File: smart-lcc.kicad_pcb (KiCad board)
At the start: 4 copper layers, 53.2 x 53.2 mm, 117 parts, among them J1 280372-1, J2 F0503-ZV-24-20T-R, J3 Conn_01x24, J4 BM04B-SRSS-TB(LF)(SN), J5 BM04B-SRSS-TB(LF)(SN), J6 Micro_SD_Card_Det2, J7 Conn_01x12, J8 BM04B-SRSS-TB(LF)(SN), Q1 2N7002, Q2 2N7002, Q4 2N7002, Q6 NTGD3148NT1G, SW1 SW_Push, SW2 SW_Push, U1 LM5050-1, U2 RP2040, U3 ESP32-S3-WROOM-1, U4 W25Q16JVSNIQ (Program Flash), U5 W25Q16JVSNIQ (Opt. Settings f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, U6 TPS82130, U7 74LVC1G125, U8 LM5050-1, Y1 XYDBPCNANF-12MHZ

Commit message: Added some very basic ordering information (more soon)
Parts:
- R26, R27: value 18K -> 18K7
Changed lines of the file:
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@@
     (descr "Resistor SMD 0402 (1005 Metric), square (rectangular) end terminal, IPC_7351 nominal, (Body size source: IPC-SM-782 page 72, https://www.pcb-3d.com/wordpress/wp-content/uploads/ipc-sm-782a_amendment_1_and_2.pdf), generated with kicad-footprint-generator")
     (tags "resistor")
+    (property "LCSC" "C102855")
     (property "Sheetfile" "smart-lcc.kicad_sch")
     (property "Sheetname" "")
@@
         (effects (font (size 1 1) (thickness 0.15)))
     )
-    (fp_text value "18K" (at 0 1.17) (layer "F.Fab")
+    (fp_text value "18K7" (at 0 1.17) (layer "F.Fab")
         (effects (font (size 1 1) (thickness 0.15)))
     )
@@
     (descr "Resistor SMD 0402 (1005 Metric), square (rectangular) end terminal, IPC_7351 nominal, (Body size source: IPC-SM-782 page 72, https://www.pcb-3d.com/wordpress/wp-content/uploads/ipc-sm-782a_amendment_1_and_2.pdf), generated with kicad-footprint-generator")
     (tags "resistor")
+    (property "LCSC" "C102855")
     (property "Sheetfile" "smart-lcc.kicad_sch")
     (property "Sheetname" "")
@@
         (effects (font (size 1 1) (thickness 0.15)))
     )
-    (fp_text value "18K" (at 0 1.17 90) (layer "F.Fab")
-        (effects (font (size 1 1) (thickness 0.15)))
-    )
+    (fp_text value "18K7" (at 0 1.17 90) (layer "F.Fab")
+        (effects (font (size 1 1) (thickness 0.15)))
+    )

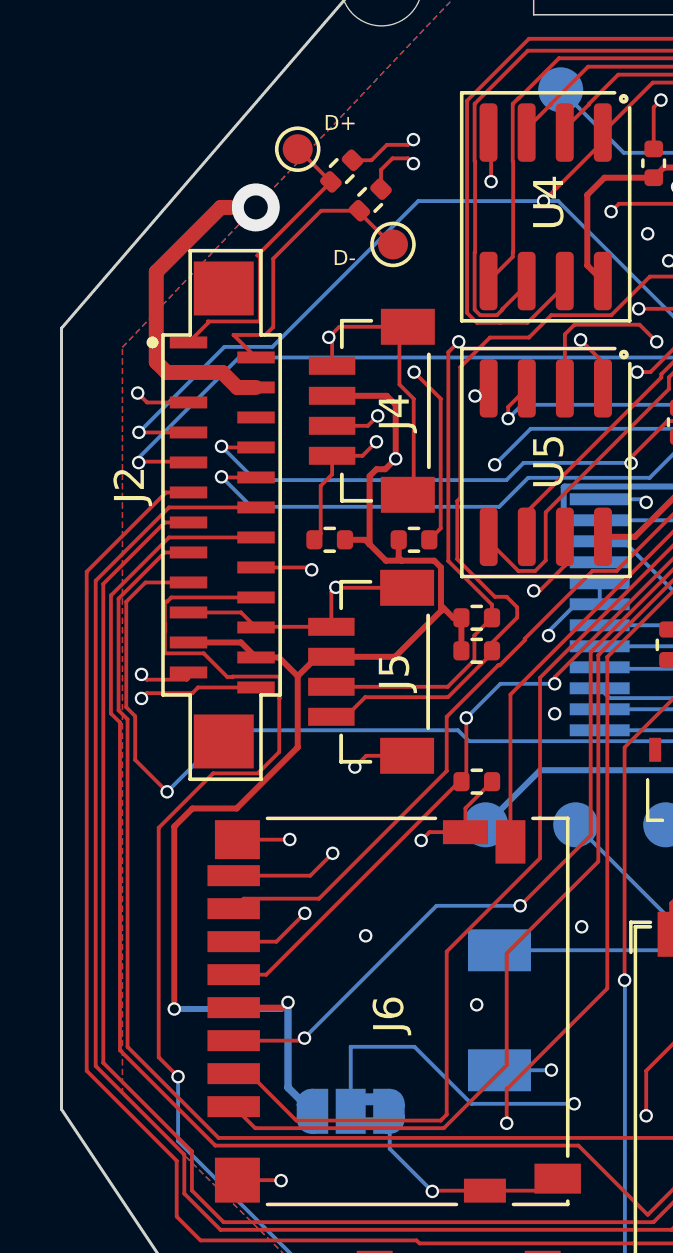
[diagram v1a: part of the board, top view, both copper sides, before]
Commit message: Updated to use a more flexible FPC connector footprint
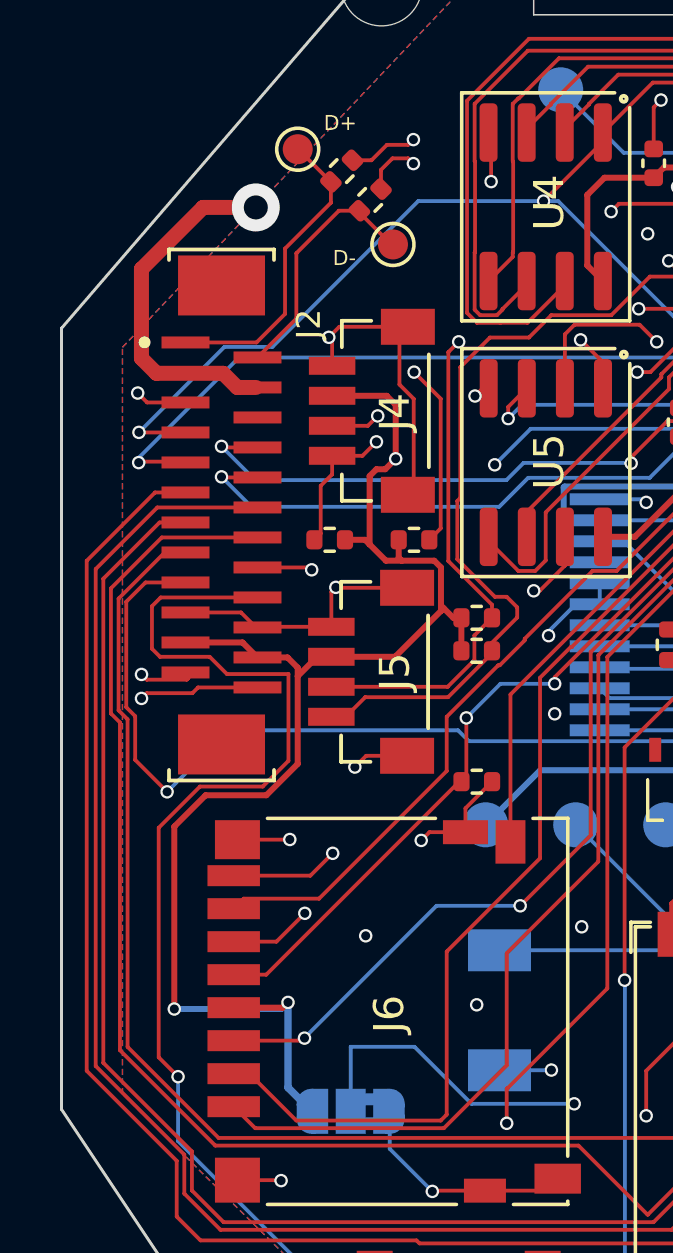
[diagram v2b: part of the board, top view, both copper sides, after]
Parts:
- J2: footprint 2N7002:FPC_24 -> FlexibleFPC:Flexible24Pin
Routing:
- net RP2040_USB_DN: track 9.94 -> 8.33 mm
- net ESP32_EN: track 88.2 -> 89.7 mm
- net VIN_DEBUG: track 66.1 -> 67.1 mm
- net +3V3: track 291.4 -> 292.0 mm

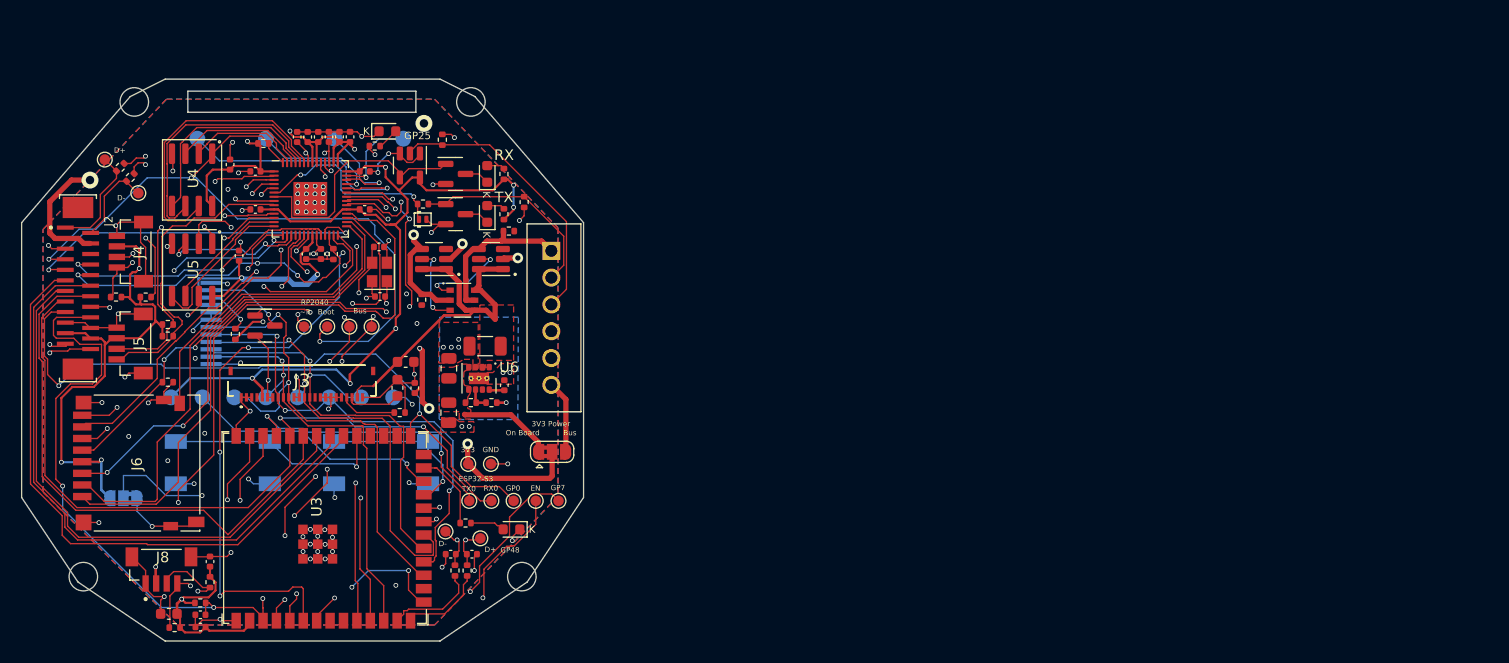
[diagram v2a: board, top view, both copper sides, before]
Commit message: R3A (preliminary)
Changes:
* Switched the OLED connector for an EyeSPI connector (feature parity with APEC)
* Removed the need for a debug board by moving USB connectors and SWD/JTAG ports to this board
* Move to 6 layers
* Component changes for a more dense design
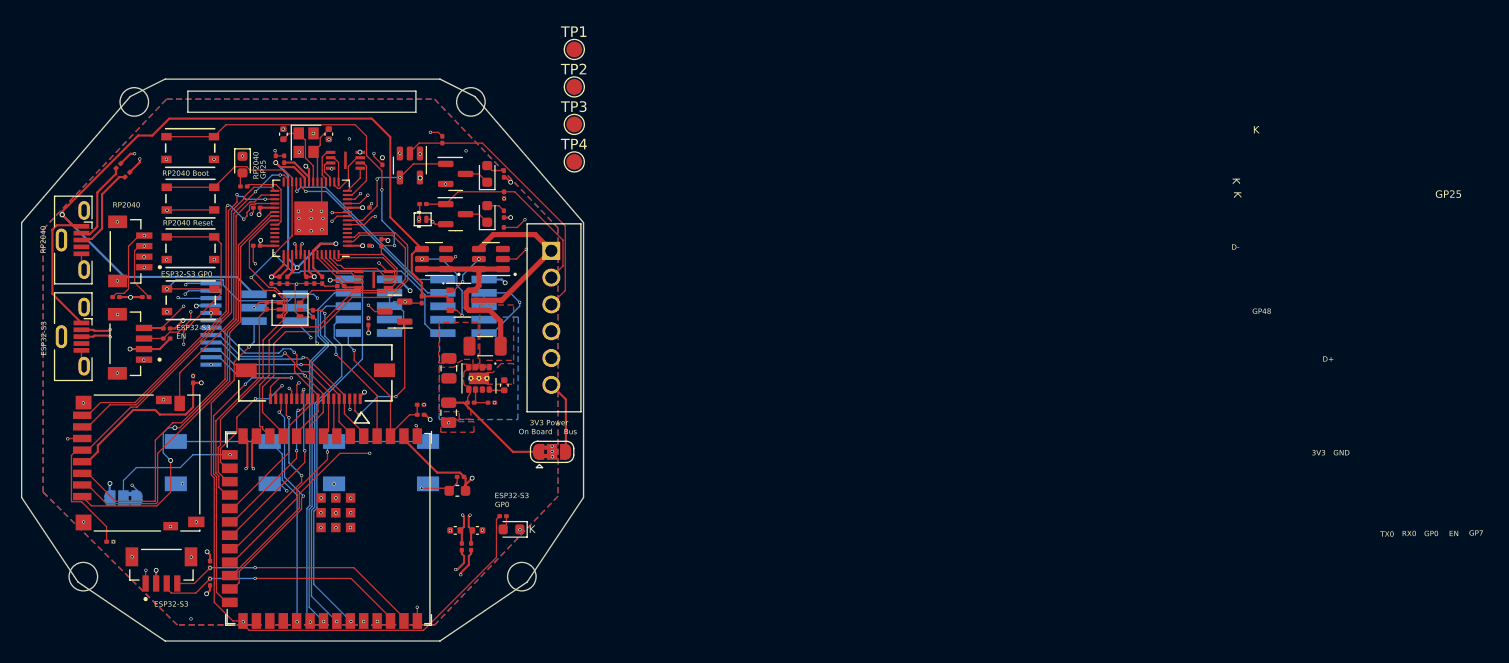
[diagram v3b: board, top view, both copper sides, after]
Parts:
- removed C1, C3: 2.2 µF / 25V, Capacitor_SMD:C_0603_1608Metric
- removed C4: 1 uF, 16V, Capacitor_SMD:C_0402_1005Metric
- removed TP10, TP28, TP29, TP5, TP6, TP7, TP8, TP9: TestPoint_Small, TestPoint:TestPoint_Pad_D1.0mm
- removed TP13, TP17, TP18: TestPoint, TestPoint:TestPoint_Pad_D1.0mm
- removed TP14, TP15, TP16, TP19: TestPoint, TestPoint:TestPoint_Pad_D1.5mm
- removed TP20, TP21, TP22, TP23, TP24, TP25, TP26, TP27: TestPoint_Small, TestPoint:TestPoint_Pad_D1.5mm
- added J10: Conn_02x05_Odd_Even, Connector_PinHeader_1.27mm:PinHeader_2x05_P1.27mm_Vertical_SMD, B.Cu at (55.8, 44.4)
- added J11: Conn_02x03_Odd_Even, Connector_PinHeader_1.27mm:PinHeader_2x03_P1.27mm_Vertical_SMD, B.Cu at (46.8, 44.5)
- added J12: Conn_01x12, TFT_1.47IN_172X320_12P:TFT_1.47IN_172X320_12P, B.Cu at (49.8, 46.0)
- added J9: Molex_0525591853, Molex_5051101892:CON_5051101892_MOL, F.Cu at (50.7, 50.7)
- added Q3: 2N7002, Package_TO_SOT_SMD:SOT-23, F.Cu at (58.2, 44.9)
- added REF**: VariegatedCoffeeLogo_Small, VariegatedCoffeeLogo:VariegatedCoffeeLogo_Small, B.Cu at (43.3, 75.8)
- added REF**: OSHW-Logo2_9.8x8mm_SilkScreen, Symbol:OSHW-Logo2_9.8x8mm_SilkScreen, B.Cu at (56.2, 70.2)
- added SW3: SW_Push, ul_PTS815-SJM-250-SMTR-LFS:SW4_PTS815 SJM 250 SMTR LFS_CNK, F.Cu at (38.8, 29.4)
- added SW4: SW_Push, ul_PTS815-SJM-250-SMTR-LFS:SW4_PTS815 SJM 250 SMTR LFS_CNK, F.Cu at (38.9, 34.2)
- added SW5: SW_Push, ul_PTS815-SJM-250-SMTR-LFS:SW4_PTS815 SJM 250 SMTR LFS_CNK, F.Cu at (38.9, 38.9)
- added SW6: SW_Push, ul_PTS815-SJM-250-SMTR-LFS:SW4_PTS815 SJM 250 SMTR LFS_CNK, F.Cu at (38.9, 43.8)
- C10, C13, C14, C15, C16, C17, C18, C19, C20, C21, C22, C24, C9: footprint Capacitor_SMD:C_0402_1005Metric -> Capacitor_SMD:C_0201_0603Metric
- C11, C12, C23, C8: value 1 uF, 16V -> 1 uF, 10V; footprint Capacitor_SMD:C_0402_1005Metric -> Capacitor_SMD:C_0201_0603Metric
- J2: value F0503-ZV-24-20T-R -> USB_B_Micro; footprint FlexibleFPC:Flexible24Pin -> Connector_USB:USB_Micro-B_Molex-105133-0001
- J3: value Conn_01x24 -> USB_B_Micro; footprint FH34SRJ-24S-0.5SH_50:FH34SRJ24S05SH50 -> Connector_USB:USB_Micro-B_Molex-105133-0001
- J7: value Conn_01x12 -> Conn_02x05_Odd_Even; footprint TFT_1.47IN_172X320_12P:TFT_1.47IN_172X320_12P -> Connector_PinHeader_1.27mm:PinHeader_2x05_P1.27mm_Vertical_SMD
- Q4: value 2N7002 -> DMN63D8LDW; footprint Package_TO_SOT_SMD:SOT-23 -> PCM_Package_TO_SOT_SMD_AKL:SOT-363_SC-70-6
- R1: value 910K -> 100R; footprint Resistor_SMD:R_0402_1005Metric -> Resistor_SMD:R_0201_0603Metric
- R10, R11, R13, R14, R15, R16, R17, R19, R2, R20, R21, R22, R23, R24, R25, R26, R27, R3, R4, R5, R6, R7, R8, R9: footprint Resistor_SMD:R_0402_1005Metric -> Resistor_SMD:R_0201_0603Metric
- R12: value 100R -> 10R; footprint Resistor_SMD:R_0402_1005Metric -> Resistor_SMD:R_0201_0603Metric
- R18: value 10R -> 4K7; footprint Resistor_SMD:R_0402_1005Metric -> Resistor_SMD:R_0201_0603Metric
- TP1, TP2, TP3, TP4: value TestPoint_Small -> TestPoint; footprint TestPoint:TestPoint_Pad_D1.0mm -> TestPoint:TestPoint_Pad_D1.5mm
- U4, U5: footprint PCM_Package_SO_AKL:SOIC-8_3.9x4.9mm_P1.27mm -> W25Q16JVUXIQ:SON50P300X200X60-9N
- moved TP1 43.5 mm to (75.2, 20.1)
- moved TP2 40.4 mm to (75.2, 23.6)
- moved TP3 36.1 mm to (75.2, 27.1)
- moved TP4 32.3 mm to (75.2, 30.7)
- moved C28 29.7 mm to (64.1, 61.9)
- moved C12 28.8 mm to (60.6, 53.7), turned to 180 degrees
- moved C24 28.4 mm to (64.4, 60.5)
- moved R9 27.4 mm to (60.6, 54.6), turned to 180 degrees
- moved J3 22.1 mm to (27.7, 47.2), turned to -90 degrees
- moved R12 21.2 mm to (55.7, 45.8), turned to 90 degrees
- moved U4 19.6 mm to (56.2, 41.8), turned to 180 degrees
- moved C7 17.9 mm to (47.6, 28.1), turned to 90 degrees
- moved U5 17.8 mm to (53.5, 30.6), turned to 0 degrees
- moved C8 17.3 mm to (39.1, 51.3)
- moved C10 16.2 mm to (57.0, 30.7), turned to 90 degrees
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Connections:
- net 12V_OLED renamed VIN_CONN
- J2 pad 1: RP2040_USB_DP -> VIN_DEBUG
- J2 pad 3: VIN_DEBUG -> RP2040_USB_DP
- J2 pad 4: VIN_DEBUG -> unconnected-(J2-ID-Pad4)
- J2 pad 6: unconnected-(J2-Pin_6-Pad6) -> GND
- J3 pad 1: GND -> VIN_DEBUG
- J3 pad 2: GND -> ESP32_USB_DN
- J3 pad 3: GND -> ESP32_USB_DP
- J3 pad 5: +3V3 -> GND
- J7 pad 1: GND -> +3V3
- J7 pad 10: SSD1309_MOSI -> RP2040_RESETn
- J7 pad 2: Net-(J7-Pin_2) -> RP2040_SWD
- J7 pad 3: Net-(J7-Pin_3) -> GND
- J7 pad 4: +3V3 -> RP2040_SWCLK
- J7 pad 6: GND -> unconnected-(J7-Pin_6-Pad6)
- J7 pad 7: SSD1309_DC -> unconnected-(J7-Pin_7-Pad7)
- J7 pad 8: SSD1309_CS -> unconnected-(J7-Pin_8-Pad8)
- J7 pad 9: SSD1309_SCLK -> GND
- Q4 pad 1: BACKLIGHT -> GND
- Q4 pad 2: GND -> ESP32_BOOTSEL_RP2040
- Q4 pad 3: Net-(J7-Pin_2) -> RP2040_RESETn
- R1 pad 1: GND -> ESP32_GPIO0
- R1 pad 2: Net-(J3-Pin_21) -> Net-(D4-A)
- R11 pad 1: RP2040_RESETn -> ESP32_BOOTSEL_RP2040
- R12 pad 1: Net-(U3-GPIO48/SPICLK_N/SUBSPICLK_N_DIFF) -> +3V3
- R12 pad 2: Net-(D4-A) -> Net-(J12-Pin_3)
- R18 pad 1: +3V3 -> ESP32_DISABLE_RP2040
- R18 pad 2: Net-(J7-Pin_3) -> GND
- TP1 pad 1: ESP32_RXD0 -> unconnected-(TP1-Pad1)
- TP2 pad 1: ESP32_TXD0 -> unconnected-(TP2-Pad1)
- TP3 pad 1: ESP32_GPIO0 -> unconnected-(TP3-Pad1)
- TP4 pad 1: ESP32_EN -> unconnected-(TP4-Pad1)
- U2 pad 18: unconnected-(U2-GPIO15-Pad18) -> RP2040_SET_CS
- U2 pad 28: RP2040_SET_CS -> unconnected-(U2-GPIO17-Pad28)
- U2 pad 38: Net-(U2-GPIO26_ADC0) -> unconnected-(U2-GPIO26_ADC0-Pad38)
- U2 pad 39: Net-(U2-GPIO27_ADC1) -> unconnected-(U2-GPIO27_ADC1-Pad39)
- U2 pad 4: RP2040_ESP32_CTS -> unconnected-(U2-GPIO2-Pad4)
- U2 pad 40: Net-(U2-GPIO28_ADC2) -> unconnected-(U2-GPIO28_ADC2-Pad40)
- U2 pad 41: Net-(U2-GPIO29_ADC3) -> unconnected-(U2-GPIO29_ADC3-Pad41)
- U2 pad 5: RP2040_ESP32_RTS -> unconnected-(U2-GPIO3-Pad5)
- U3 pad 10: RP2040_ESP32_RX -> SSD1309_CS
- U3 pad 11: RP2040_ESP32_TX -> RP2040_ESP32_RX
- U3 pad 12: SSD1309_RES -> RP2040_ESP32_TX
- U3 pad 17: SSD1309_DC -> RP2040_SERIAL_BOOT
- U3 pad 18: SSD1309_CS -> ESP32_BOOTSEL_RP2040
- U3 pad 19: SSD1309_MOSI -> ESP32_EYESPI_SD_CS
- U3 pad 20: SSD1309_SCLK -> ESP32_EYESPI_MEM_CS
- U3 pad 21: RP2040_ESP32_RTS -> ESP32_EYESPI_TS_CS
- U3 pad 22: RP2040_ESP32_CTS -> ESP32_EYESPI_INT
- U3 pad 25: Net-(U3-GPIO48/SPICLK_N/SUBSPICLK_N_DIFF) -> ESP32_EYESPI_BUSY_TE
- U3 pad 4: RP2040_RESETn -> ESP32_DISABLE_RP2040
- U3 pad 5: RP2040_BOOTSEL -> SSD1309_SCLK
- U3 pad 6: RP2040_SERIAL_BOOT -> SSD1309_MOSI
- U3 pad 7: Net-(U3-GPIO7/TOUCH7/ADC1_CH6) -> ESP32_GPIO7
- U3 pad 8: ESP32_RTS0 -> SSD1309_DC
- U3 pad 9: ESP32_CTS0 -> SSD1309_RES
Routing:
- net +3V3: track 292.0 -> 75.8 mm, vias 20 -> 33
- net GND: track 173.6 -> 80.4 mm, vias 93 -> 87
- net ESP32_EN: track 89.7 -> 42.9 mm, vias 4 -> 3
- net RP2040_BOOTSEL: track 96.8 -> 50.8 mm, vias 6 -> 2
- net RP2040_ESP32_RTS: track 41.9 -> 0.00 mm, vias 2 -> 0
- net RP2040_ESP32_CTS: track 41.4 -> 0.00 mm, vias 2 -> 0
- net ESP32_RXD0: track 73.2 -> 32.9 mm
- net RP2040_SERIAL_BOOT: track 64.1 -> 31.2 mm, vias 5 -> 0
- net ESP32_GPIO45: track 0.00 -> 30.8 mm, vias 0 -> 2
- net Net-(U3-GPIO7/TOUCH7/ADC1_CH6): track 30.4 -> 0.00 mm, vias 2 -> 0
- net RP2040_SD_DAT1: track 63.8 -> 33.9 mm
- net SSD1309_DC: track 48.8 -> 19.0 mm, vias 2 -> 1
- net Net-(JP1-C): track 40.6 -> 12.8 mm, vias 3 -> 1
- net RP2040_ESP32_TX: track 61.9 -> 34.5 mm, vias 4 -> 0
- net SSD1309_CS: track 45.1 -> 18.0 mm, vias 3 -> 1
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- added copper zone on In1.Cu, net +3V3
- added copper zone on In3.Cu, net GND
- added copper zone on In4.Cu, net GND
- removed copper zone on In1.Cu, net GND
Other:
- copper layers 4 -> 6
- board text added: "ESP-Debug"
- board text added: "ESP32 JTAG"
- board text added: "ESP32-S3 EN"
- board text added: "ESP32-S3 GP0"
- board text added: "RP2040 Boot"
- board text added: "RP2040 Reset"
- board text added: "RP2040 SWD"
- board text added: "Rev R3A"
- board text added: "variegated.coffee/open-lcc"
- board text removed: "BL"
- board text removed: "Boot"
- board text removed: "CK"
- board text removed: "CS"
- board text removed: "DC"
- board text removed: "GP26"
- board text removed: "GP27"
- board text removed: "GP28"
- board text removed: "GP29"
- board text removed: "Licensed under CERN-OHL-P v2"
- board text removed: "MO"
- board text removed: "RES"
- board text removed: "RP2040 GPIO"
- board text removed: "Rev R2C"
- board text removed: "github.com/open-lcc/open-lcc-board"
- board text removed: "~R"
